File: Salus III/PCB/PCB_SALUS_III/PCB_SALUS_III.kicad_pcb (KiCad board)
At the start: 2 copper layers, 43 parts, among them K1 Relay_SPDT, U1 ESP32-DEVKITC-32D, U2 RASPBERRY_PI_4B_4GB

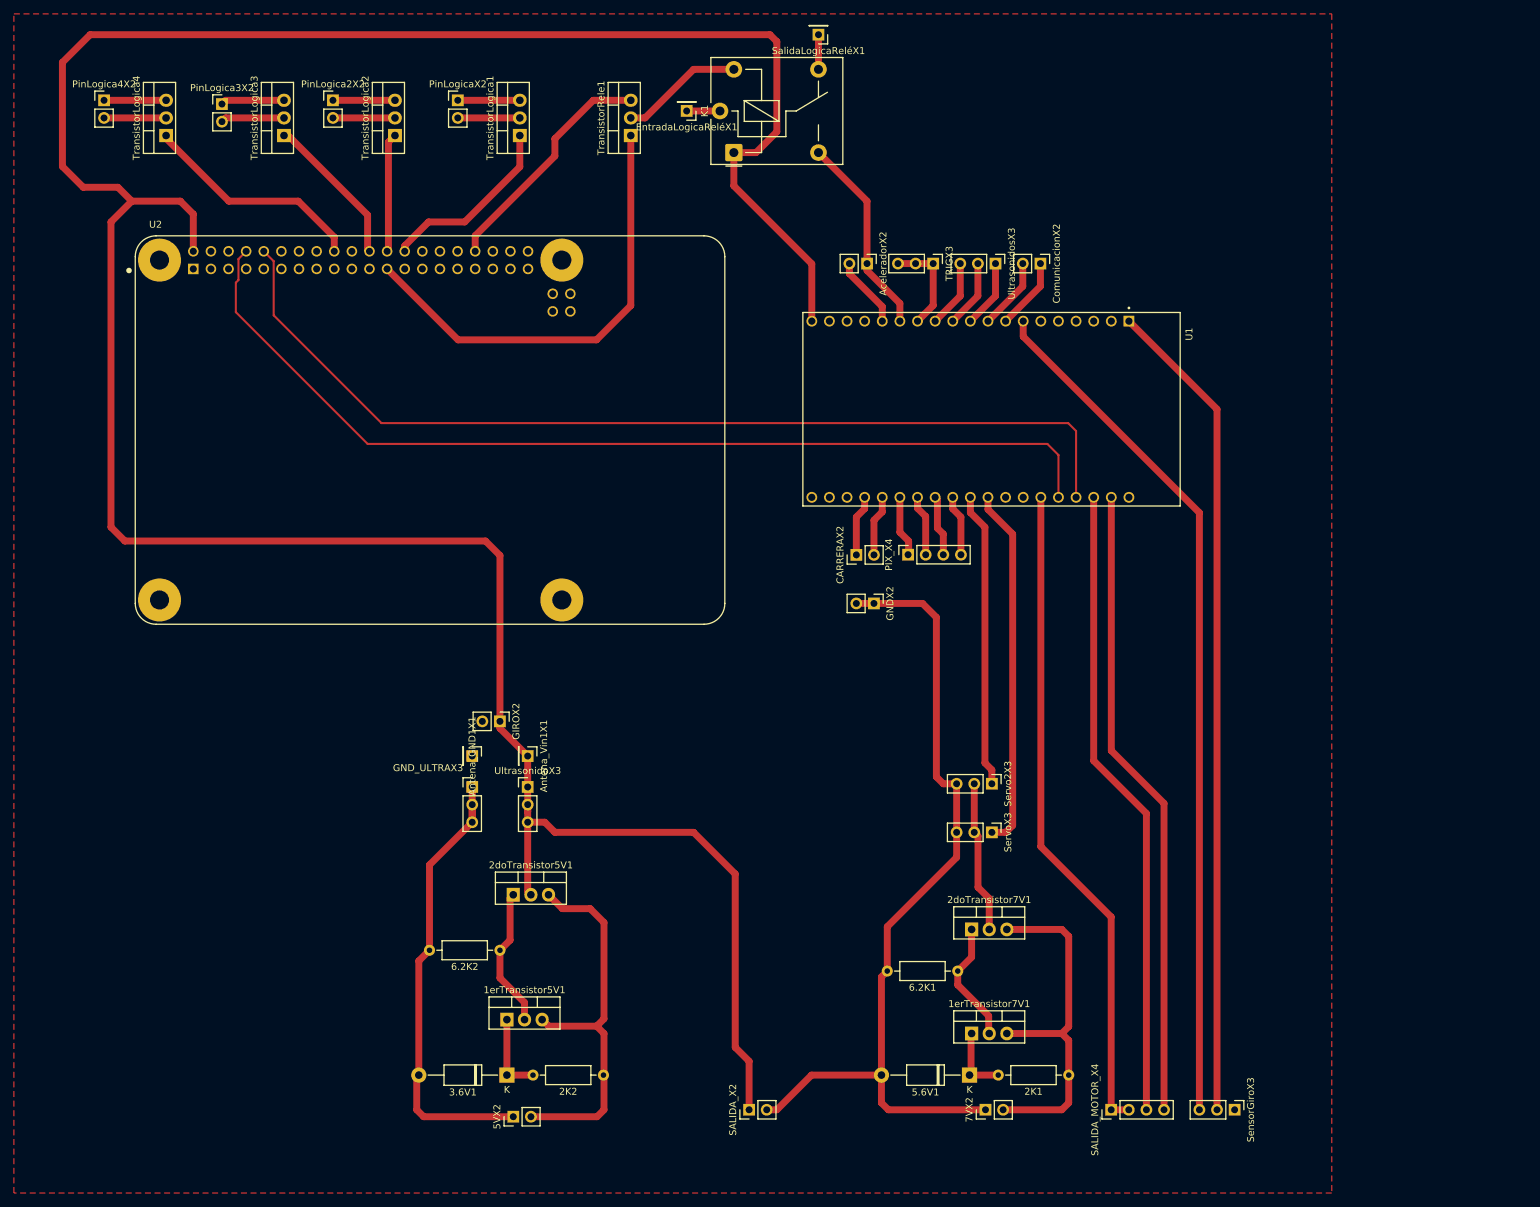
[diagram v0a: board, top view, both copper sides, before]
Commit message: Parece ser la PCB definitiva de SALUS III por lo menos parte logica
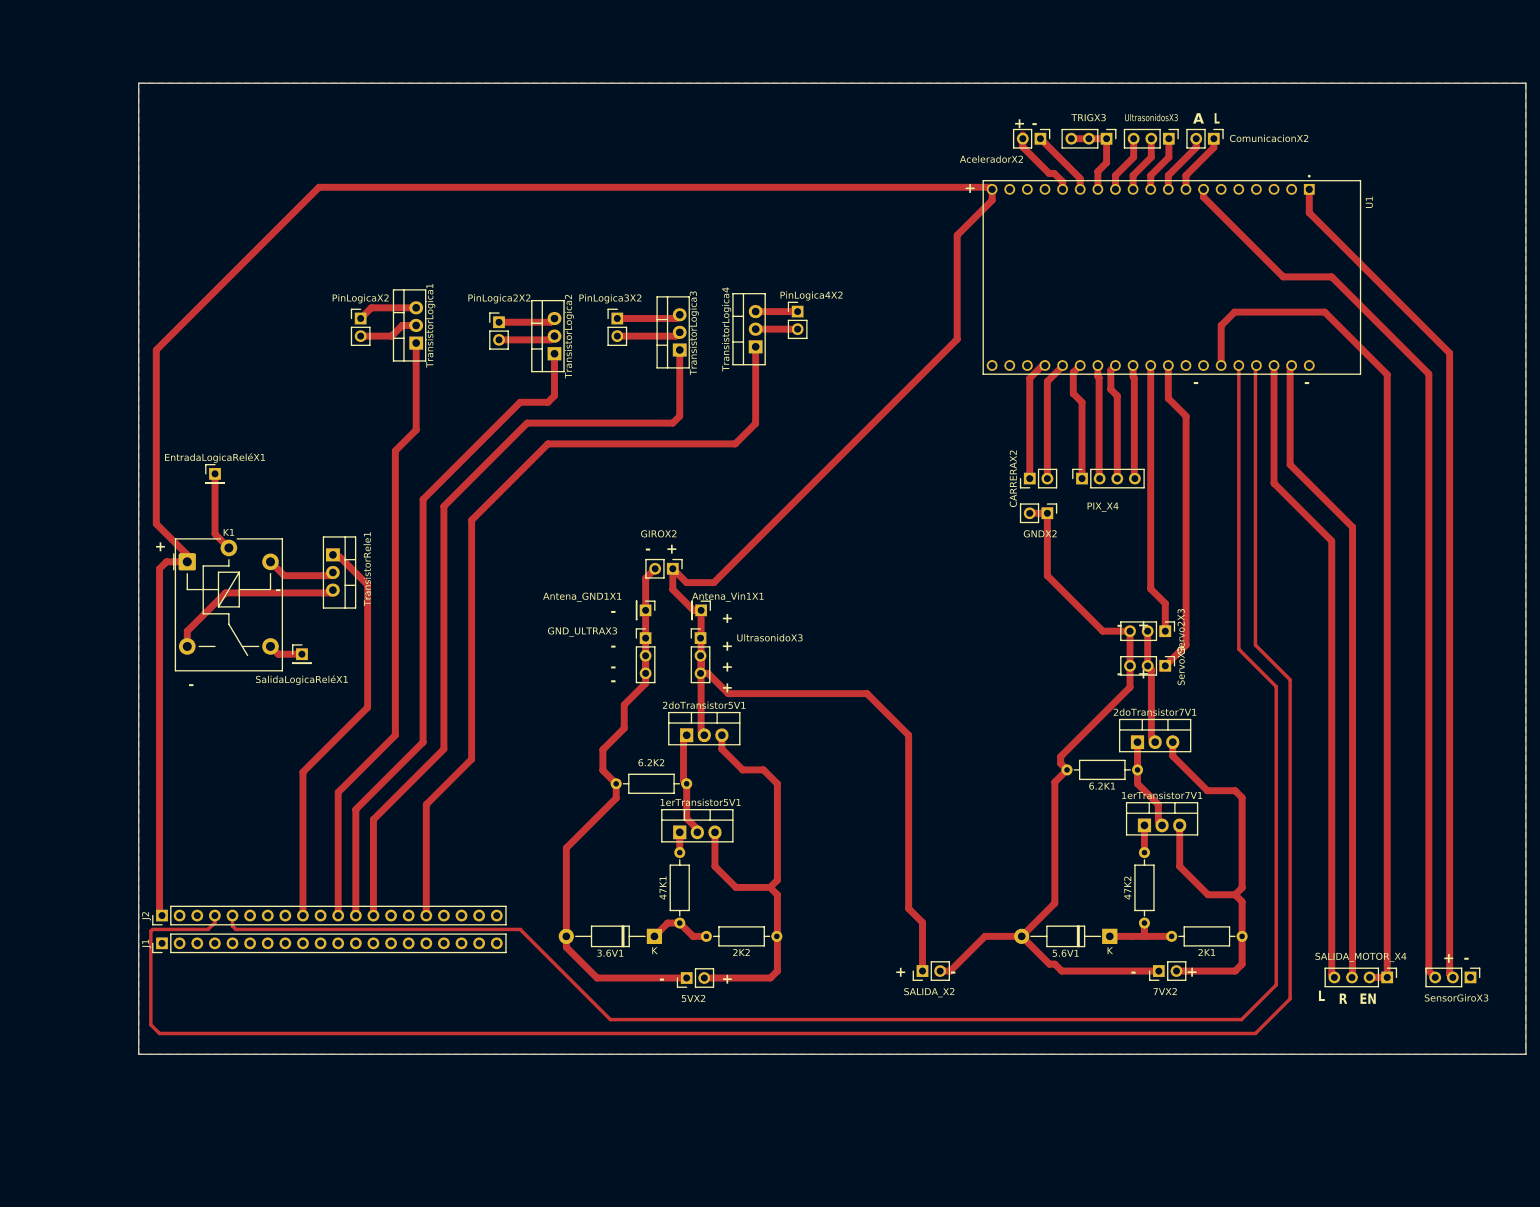
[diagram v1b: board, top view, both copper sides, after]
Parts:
- removed U2: RASPBERRY_PI_4B_4GB, Huella_Rasp:MODULE_RASPBERRY_PI_4B_4GB
- added 47K1: Resistencia Base 5V, Resistor_THT:R_Axial_DIN0207_L6.3mm_D2.5mm_P10.16mm_Horizontal, F.Cu at (108.0, 143.1)
- added 47K2: Resistencia Base 7V, Resistor_THT:R_Axial_DIN0207_L6.3mm_D2.5mm_P10.16mm_Horizontal, F.Cu at (175.0, 143.1)
- added J1: Conn_01x20_Pin, Connector_PinHeader_2.54mm:PinHeader_1x20_P2.54mm_Vertical, F.Cu at (33.4, 146.0)
- added J2: Conn_01x20_Pin, Connector_PinHeader_2.54mm:PinHeader_1x20_P2.54mm_Vertical, F.Cu at (33.4, 142.0)
- moved SalidaLogicaReléX1 116.3 mm to (53.5, 104.3), turned to 0 degrees
- moved PinLogica4X2 104.5 mm to (125.0, 54.9)
- moved K1 98.4 mm to (37.0, 91.0), turned to 0 degrees
- moved TransistorLogica4 90.3 mm to (118.9, 60.0)
- moved EntradaLogicaReléX1 85.8 mm to (41.0, 78.3), turned to 0 degrees
- moved TransistorRele1 74.2 mm to (58.0, 90.0), turned to -90 degrees
- moved TransistorLogica3 64.9 mm to (108.0, 60.5)
- moved PinLogica3X2 64.8 mm to (99.0, 55.9)
- moved SALIDA_MOTOR_X4 44.1 mm to (210.0, 150.9), turned to -90 degrees
- moved PinLogica2X2 40.0 mm to (81.9, 56.5)
- moved 1erTransistor7V1 39.0 mm to (175.0, 129.0)
- moved SensorGiroX3 39.0 mm to (222.0, 150.9)
- moved TransistorLogica2 39.0 mm to (89.9, 61.0)
- moved 6.2K1 38.9 mm to (174.0, 121.0)
- moved 1erTransistor5V1 36.7 mm to (108.0, 130.0)
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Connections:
- 2K1 pad 2: Net-(1erTransistor7V1-G) -> Net-(5.6V1-K)
- 2K2 pad 2: Net-(1erTransistor5V1-G) -> Net-(3.6V1-K)
- 3.6V1 pad 1: Net-(1erTransistor5V1-G) -> Net-(3.6V1-K)
- 5.6V1 pad 1: Net-(1erTransistor7V1-G) -> Net-(5.6V1-K)
- U1 pad J3-2: L_PWM -> R_PWM
- U1 pad J3-3: R_PWM -> L_PWM
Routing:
- net TX_ESP: track 142.0 -> 284.5 mm
- net RX_ESP: track 142.6 -> 251.2 mm
- net Net-(J2-Pin_13): track 22.1 -> 112.1 mm
- net Net-(J2-Pin_16): track 32.6 -> 117.5 mm
- net Net-(J2-Pin_12): track 17.2 -> 95.2 mm
- net Net-(J2-Pin_11): track 26.6 -> 87.2 mm
- net M_EN: track 95.0 -> 123.7 mm
- net 5V: track 422.2 -> 395.0 mm
- net GND: track 253.3 -> 232.2 mm
- net Net-(1erTransistor7V1-S): track 52.0 -> 64.8 mm
- net Net-(5.6V1-K): track 0.00 -> 10.8 mm
- net Net-(3.6V1-K): track 0.00 -> 9.08 mm
- net Net-(1erTransistor5V1-G): track 11.8 -> 2.92 mm
- net Net-(CARRERAX2-Pin_1): track 8.80 -> 17.4 mm
- net Net-(CARRERAX2-Pin_2): track 8.80 -> 17.2 mm
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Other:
- board outline added: 200 x 140 mm
- board text added: "+"
- board text added: "-"
- board text added: "A"
- board text added: "EN"
- board text added: "L"
- board text added: "R"

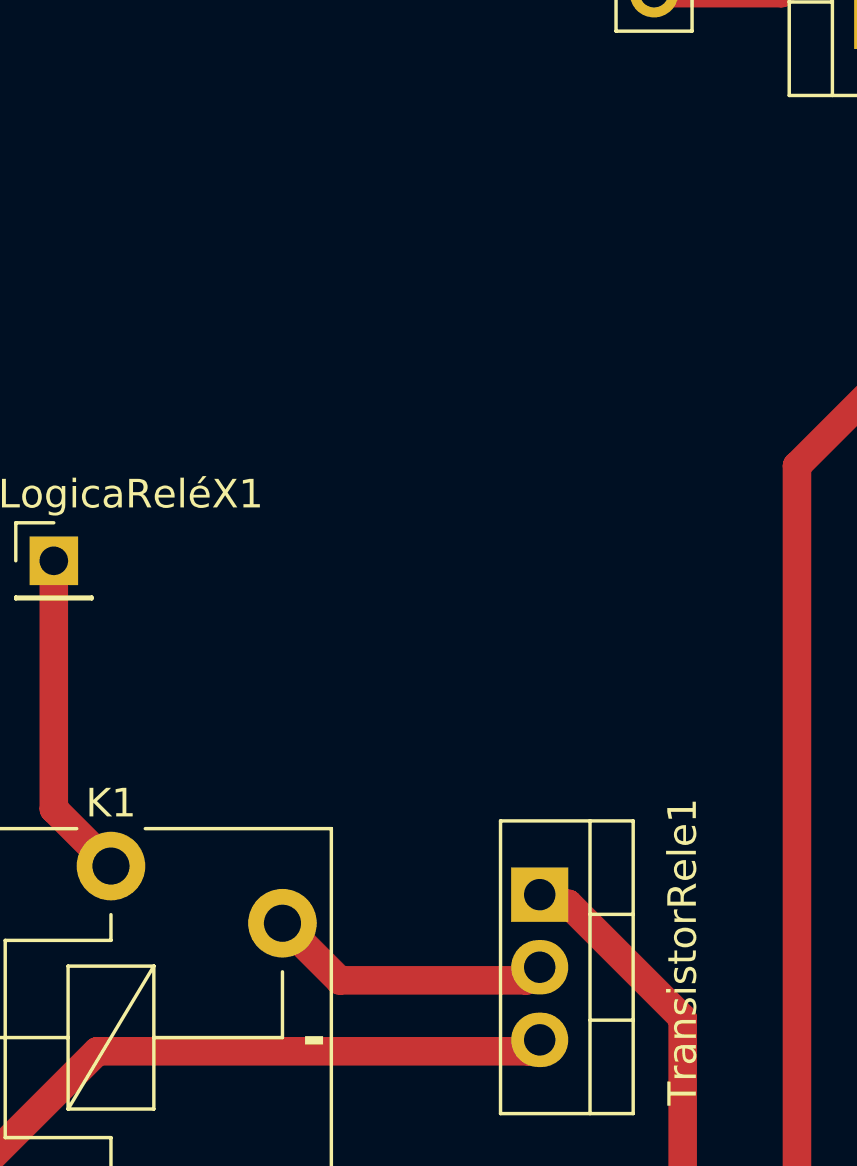
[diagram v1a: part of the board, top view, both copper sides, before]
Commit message: se agrego el diodo TVS a probar para proteger de cierres de Relé
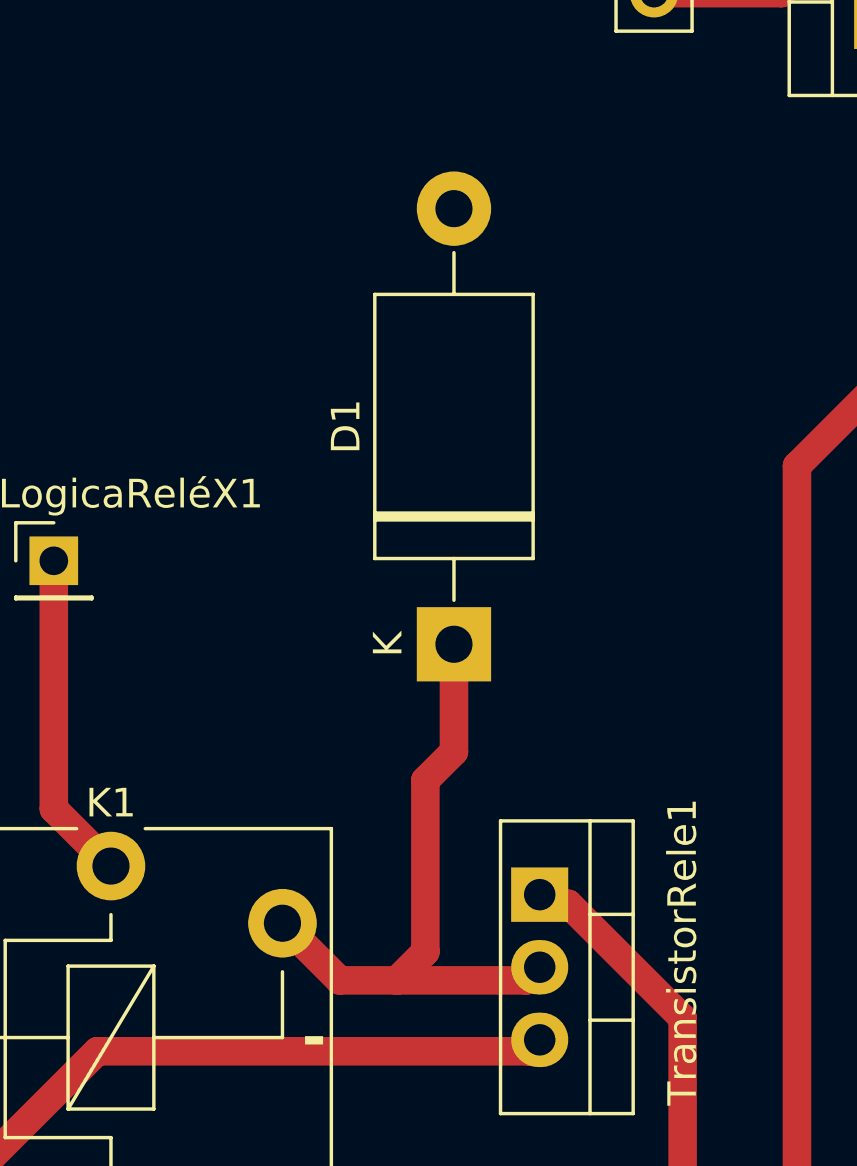
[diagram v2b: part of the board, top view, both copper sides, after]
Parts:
- added D1: 1N62xxA, Diode_THT:D_DO-201AE_P15.24mm_Horizontal, F.Cu at (55.0, 81.2)
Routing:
- net Net-(D1-A1): track 10.0 -> 22.6 mm

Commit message: PCB Hecha para ser enviada a China, falta revisar que esten todas las conexiones
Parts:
- Entrada Arranque: renamed from SalidaLogicaReléX1
- Servo 1: renamed from ServoX3
- Servo 2: renamed from Servo2X3
- moved EntradaLogicaReléX1 237.9 mm to (269.1, 145.8)
- moved Arranque 236.1 mm to (268.4, 138.0), turned to 180 degrees
- moved 5VX2 227.1 mm to (332.2, 109.0), turned to 180 degrees
- moved J2 226.5 mm to (244.0, 58.6), turned to 0 degrees
- moved J1 224.3 mm to (240.0, 58.6), turned to 0 degrees
- moved 3.6V1 217.2 mm to (320.1, 119.2), turned to 0 degrees
- moved Entrada Arranque 214.9 mm to (264.4, 145.8)
- moved 47K1 214.3 mm to (318.8, 104.4), turned to -90 degrees
- moved 2K2 214.3 mm to (331.4, 99.5)
- moved 1erTransistor5V1 206.0 mm to (313.3, 113.1), turned to 90 degrees
- moved PinLogicaX2 200.1 mm to (261.9, 65.0), turned to -90 degrees
- moved SALIDA 197.9 mm to (331.7, 90.4), turned to 180 degrees
- moved 6.2K2 196.4 mm to (305.3, 116.6), turned to -90 degrees
- moved D1 195.7 mm to (244.3, 130.9), turned to -90 degrees
- moved 2doTransistor5V1 190.0 mm to (299.0, 113.2), turned to 90 degrees
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- renumbered AceleradorX2 to Acelerador, Antena_Vin1X1 to Antena, Antena_GND1X1 to Antena, K1 to Arranque, U1 to ESP32, CARRERAX2 to FC, GNDX2 to FCGND, GIROX2 to GIRO, ComunicacionX2 to IIC, PIX_X4 to PIX, SALIDA_X2 to SALIDA, SALIDA_MOTOR_X4 to SALIDA_MOTOR, TRIGX3 to Trig, UltrasonidosX3 to Ultrasonidos
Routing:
- net TX_ESP: track 284.5 -> 73.2 mm
- net 5V: track 395.0 -> 207.2 mm, vias 0 -> 7
- net RX_ESP: track 251.2 -> 71.6 mm
- net Net-(SensorGiroX3-Pin_2): track 122.2 -> 14.9 mm
- net Net-(J2-Pin_16): track 117.5 -> 15.9 mm, vias 0 -> 1
- net Net-(J2-Pin_13): track 112.1 -> 12.9 mm
- net Net-(SensorGiroX3-Pin_3): track 131.6 -> 32.4 mm
- net M_EN: track 123.7 -> 43.4 mm, vias 0 -> 1
- net Net-(J2-Pin_12): track 95.2 -> 25.7 mm, vias 0 -> 3
- net R_PWM: track 92.1 -> 27.3 mm, vias 0 -> 1
- net L_PWM: track 91.8 -> 27.7 mm, vias 0 -> 1
- net Net-(ServoX3-Pin_1): track 45.6 -> 97.8 mm, vias 0 -> 4
- net Net-(J2-Pin_11): track 87.2 -> 37.6 mm, vias 0 -> 2
- net Net-(SalidaLogicaReléX1-Pin_1): track 5.00 -> 39.3 mm, vias 0 -> 2
- net Net-(Servo2X3-Pin_1): track 39.2 -> 69.1 mm, vias 0 -> 3
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- added copper zone on B.Cu, net GND
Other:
- board size 200 x 140 mm -> 100 x 100 mm
- board text added: "B"

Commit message: Mandar a China
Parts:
- removed SensorGiroX3: Sensor de Giro, Connector_PinHeader_2.54mm:PinHeader_1x03_P2.54mm_Vertical
- added G***: LOGO, Logo:Logo, B.Cu at (318.2, 131.7)
- added Giro1: Conn_01x02_Pin, Connector_PinHeader_2.54mm:PinHeader_1x02_P2.54mm_Vertical, F.Cu at (325.4, 52.6)
- added Pan1: Conn_01x03_Pin, Connector_PinHeader_2.54mm:PinHeader_1x03_P2.54mm_Vertical, F.Cu at (272.7, 95.8)
- added PinesAnalogicos1: Conn_01x03_Pin, Connector_PinHeader_2.54mm:PinHeader_1x03_P2.54mm_Vertical, F.Cu at (331.9, 61.2)
- added SensorCorriente1: Conn_01x03_Pin, Connector_PinHeader_2.54mm:PinHeader_1x03_P2.54mm_Vertical, F.Cu at (331.8, 78.5)
- added SensorTemperatura1: Conn_01x04_Pin, Connector_PinHeader_2.54mm:PinHeader_1x04_P2.54mm_Vertical, F.Cu at (303.5, 53.5)
- added Tilt1: Conn_01x03_Pin, Connector_PinHeader_2.54mm:PinHeader_1x03_P2.54mm_Vertical, F.Cu at (280.4, 99.8)
- SalidaLogicaReléX1: renamed from Entrada Arranque
- Servo2X3: renamed from Servo 2
- ServoX3: renamed from Servo 1
- moved SALIDA_MOTOR_X4 4.46 mm to (331.9, 65.8)
- moved J1 2.01 mm to (242.0, 58.8)
- moved J2 1.61 mm to (245.6, 58.8)
- moved SalidaLogicaReléX1 1.10 mm to (265.5, 145.8)
- moved Antena_Vin1X1 0.31 mm to (280.6, 108.6)
- moved Antena_GND1X1 0.30 mm to (280.7, 113.7)
- moved TransistorLogica4 0.29 mm to (254.1, 103.4)
- renumbered Acelerador to AceleradorX2, Antena to Antena_GND1X1, Antena to Antena_Vin1X1, FC to CARRERAX2, IIC to ComunicacionX2, GIRO to GIROX2, FCGND to GNDX2, Arranque to K1, PIX to PIX_X4, SALIDA_MOTOR to SALIDA_MOTOR_X4, SALIDA to SALIDA_X2, Trig to TRIGX3, ESP32 to U1, Ultrasonidos to UltrasonidosX3
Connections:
- J1 pad 2: unconnected-(J1-Pin_2-Pad2) -> Net-(J1-Pin_2)
- J2 pad 12: Net-(J2-Pin_12) -> unconnected-(J2-Pin_12-Pad12)
- J2 pad 13: Net-(J2-Pin_13) -> unconnected-(J2-Pin_13-Pad13)
- J2 pad 18: unconnected-(J2-Pin_18-Pad18) -> Net-(J2-Pin_18)
- J2 pad 6: unconnected-(J2-Pin_6-Pad6) -> Net-(J2-Pin_6)
- J2 pad 8: unconnected-(J2-Pin_8-Pad8) -> Net-(J2-Pin_8)
- TransistorLogica1 pad 1: Net-(J2-Pin_11) -> Net-(J2-Pin_9)
- TransistorLogica2 pad 1: Net-(J2-Pin_12) -> Net-(J2-Pin_11)
- TransistorLogica3 pad 1: Net-(J2-Pin_13) -> Net-(J2-Pin_18)
- TransistorLogica4 pad 1: Net-(J2-Pin_16) -> Net-(J1-Pin_2)
- TransistorRele1 pad 1: Net-(J2-Pin_9) -> Net-(J2-Pin_8)
- U1 pad J2-4: unconnected-(U1-SENSOR_VN-PadJ2-4) -> Net-(PinesAnalogicos1-Pin_1)
- U1 pad J2-5: unconnected-(U1-IO34-PadJ2-5) -> Net-(PinesAnalogicos1-Pin_2)
- U1 pad J2-6: unconnected-(U1-IO35-PadJ2-6) -> Net-(PinesAnalogicos1-Pin_3)
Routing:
- net 5V: track 207.2 -> 286.4 mm, vias 7 -> 8
- net Net-(J1-Pin_2): track 0.00 -> 69.7 mm, vias 0 -> 2
- net Net-(J2-Pin_6): track 0.00 -> 58.1 mm
- net Net-(J2-Pin_8): track 0.00 -> 53.5 mm, vias 0 -> 1
- net Net-(PinesAnalogicos1-Pin_3): track 0.00 -> 30.7 mm
- net Net-(PinesAnalogicos1-Pin_2): track 0.00 -> 27.7 mm
- net Net-(J2-Pin_16): track 15.9 -> 41.9 mm, vias 1 -> 3
- net Net-(J2-Pin_12): track 25.7 -> 0.00 mm, vias 3 -> 0
- net Net-(PinesAnalogicos1-Pin_1): track 0.00 -> 25.5 mm
- net Net-(J2-Pin_9): track 49.3 -> 27.7 mm
- net Net-(J2-Pin_18): track 0.00 -> 20.3 mm
- net Net-(SensorCorriente1-Pin_2): track 14.9 -> 34.2 mm, vias 0 -> 2
- net Net-(SensorCorriente1-Pin_3): track 32.4 -> 48.1 mm, vias 0 -> 1
- net Net-(J2-Pin_11): track 37.6 -> 22.8 mm, vias 2 -> 1
- net Net-(J2-Pin_13): track 12.9 -> 0.00 mm
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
